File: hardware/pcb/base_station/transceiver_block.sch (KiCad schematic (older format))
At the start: 22 parts, among them CON5 RJ45_TART, CON6 RJ45_TART, IC13 LTC2851, IC14 LTC2851, IC15 LTC2851, IC16 LTC2851, IC17 LTC2851, IC18 LTC2851

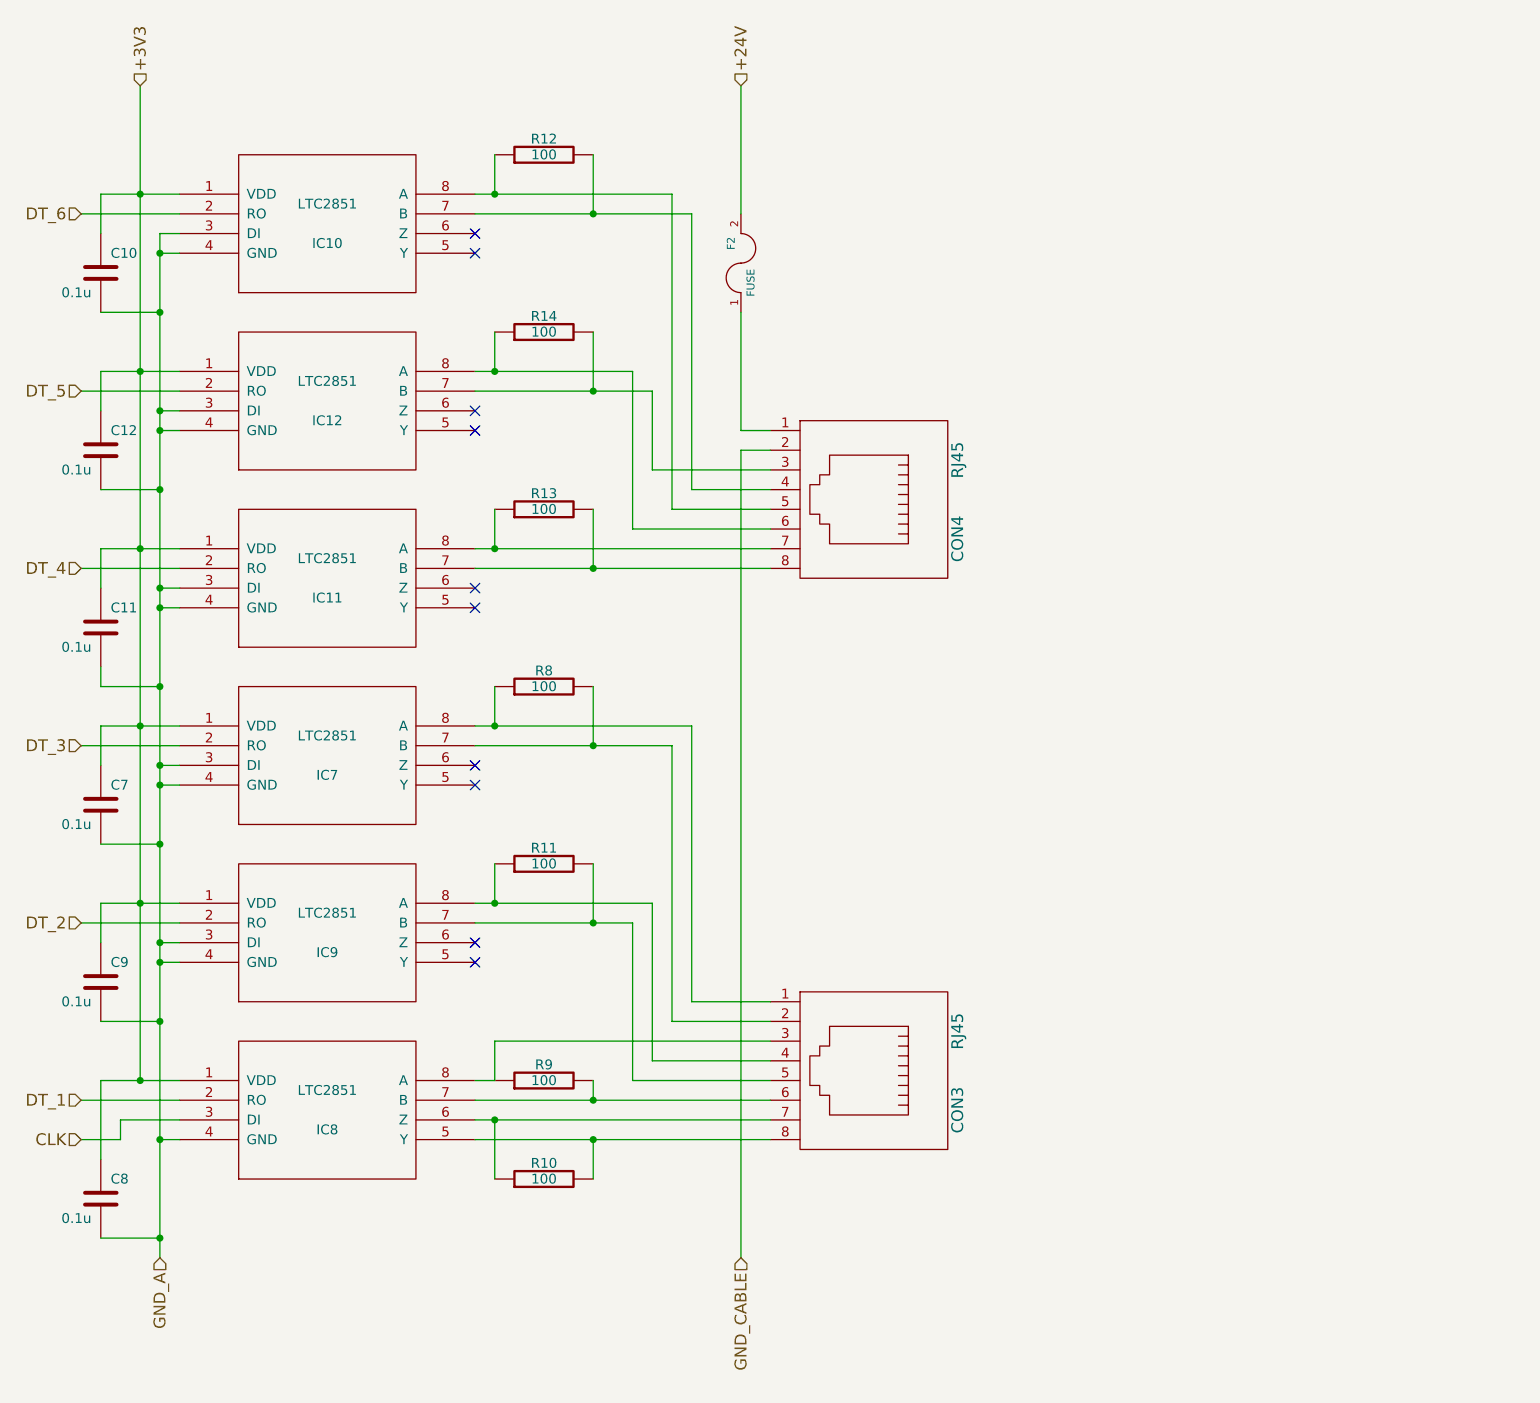
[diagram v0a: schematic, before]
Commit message: Moved things around so that old files are in the legacy directory
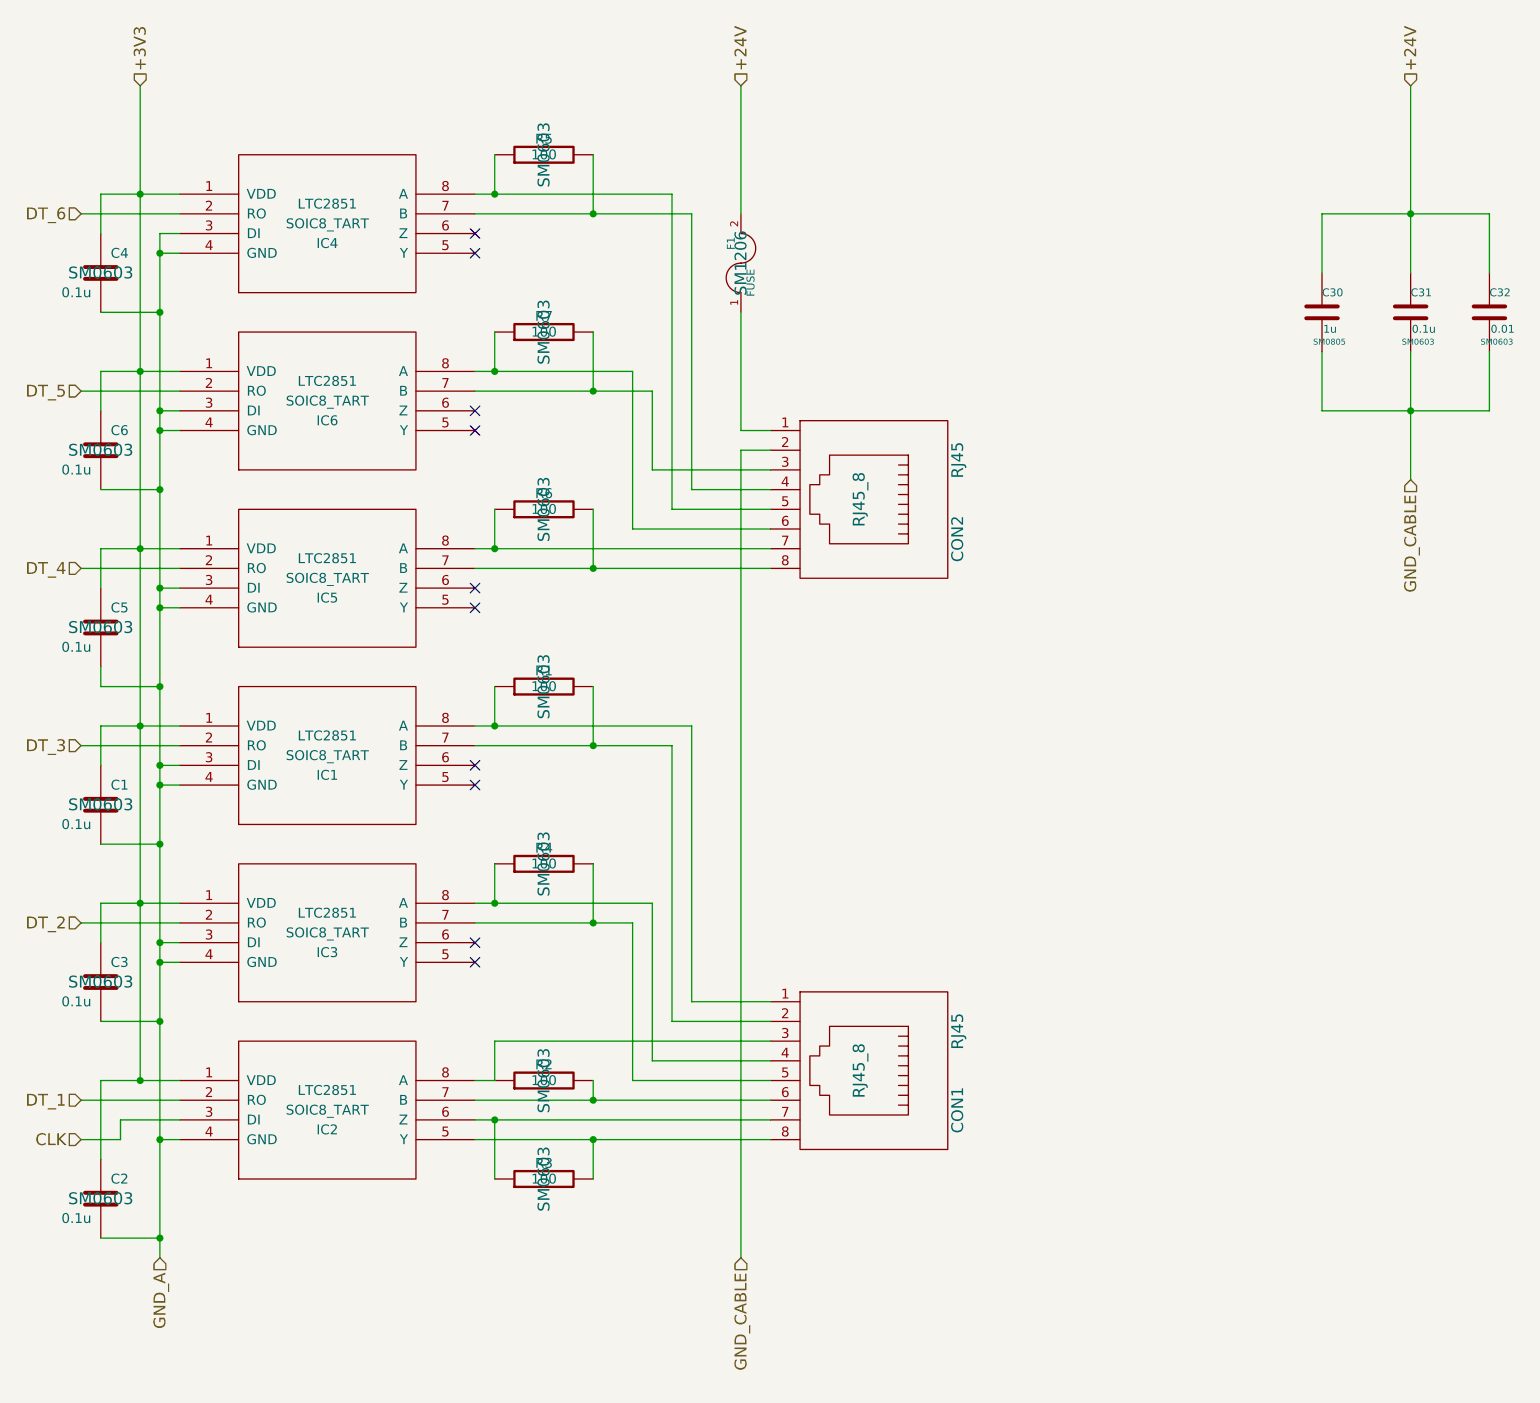
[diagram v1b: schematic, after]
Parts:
- added C36: 1u, SM0805, symbol C
- added C37: 0.1u, SM0603, symbol C
- added C38: 0.01, SM0603, symbol C
- C13, C14, C15, C16, C17, C18, R15, R16, R17, R18, R19, R20, R21: footprint (none) -> SM0603
- CON5, CON6: footprint (none) -> RJ45_8
- F1: footprint ~ -> SM1206
- IC13, IC14, IC15, IC16, IC17, IC18: footprint MODULE -> SOIC8_TART
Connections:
- net +24V: now also C36.1, C37.1, C38.1
- net GND_CABLE: now also C36.2, C37.2, C38.2
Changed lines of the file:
@@
 $Descr A4 11693 8268
 encoding utf-8
-Sheet 5 7
+Sheet 4 7
 Title ""
-Date "8 dec 2014"
+Date "13 feb 2015"
 Rev ""
 Comp ""
@@
 AR Path="/54092498/5422055D" Ref="C11"  Part="1"
 AR Path="/540670D5/5422055D" Ref="C23"  Part="1"
-F 0 "C11" H 1850 3900 50  0000 L CNN
+F 0 "C5" H 1850 3900 50  0000 L CNN
 F 1 "0.1u" H 1600 3700 50  0000 L CNN
-F 2 "" H 1800 3800 60  0001 C CNN
+F 2 "SM0603" H 1800 3800 60  0000 C CNN
 F 3 "" H 1800 3800 60  0001 C CNN
 	1    1800 3800
@@
 AR Path="/54092498/5418D866" Ref="CON3"  Part="1"
 AR Path="/540670D5/5418D866" Ref="CON7"  Part="1"
-F 0 "CON3" H 5850 6550 60  0000 C CNN
+F 0 "CON1" H 5850 6550 60  0000 C CNN
 F 1 "RJ45_TART" H 6250 6600 60  0001 C CNN
-F 2 "" H 5650 6050 60  0001 C CNN
+F 2 "RJ45_8" H 5650 6050 60  0000 C CNN
 F 3 "" H 5650 6050 60  0001 C CNN
 F 4 "STEWART CONNECTOR" H 6650 6500 60  0001 C CNN "MANUFAC"
@@
 AR Path="/54092498/5418D832" Ref="CON4"  Part="1"
 AR Path="/540670D5/5418D832" Ref="CON8"  Part="1"
-F 0 "CON4" H 5850 3650 60  0000 C CNN
+F 0 "CON2" H 5850 3650 60  0000 C CNN
 F 1 "RJ45_TART" H 6250 3700 60  0001 C CNN
-F 2 "" H 5650 3150 60  0001 C CNN
+F 2 "RJ45_8" H 5650 3150 60  0000 C CNN
 F 3 "" H 5650 3150 60  0001 C CNN
 F 4 "STEWART CONNECTOR" H 6650 3600 60  0001 C CNN "MANUFAC"
@@
 AR Path="/54092498/540678BD" Ref="R12"  Part="1"
 AR Path="/540670D5/540678BD" Ref="R26"  Part="1"
-F 0 "R12" V 4130 1400 50  0000 C CNN
+F 0 "R5" V 4130 1400 50  0000 C CNN
 F 1 "100" V 4050 1400 50  0000 C CNN
-F 2 "" H 4050 1400 60  0001 C CNN
+F 2 "SM0603" H 4050 1400 60  0000 C CNN
 F 3 "" H 4050 1400 60  0001 C CNN
 	1    4050 1400
@@
 AR Path="/54092498/540678A5" Ref="R14"  Part="1"
 AR Path="/540670D5/540678A5" Ref="R28"  Part="1"
-F 0 "R14" V 4130 2300 50  0000 C CNN
+F 0 "R7" V 4130 2300 50  0000 C CNN
 F 1 "100" V 4050 2300 50  0000 C CNN
-F 2 "" H 4050 2300 60  0001 C CNN
+F 2 "SM0603" H 4050 2300 60  0000 C CNN
 F 3 "" H 4050 2300 60  0001 C CNN
 	1    4050 2300
@@
 AR Path="/54092498/5406788C" Ref="R13"  Part="1"
 AR Path="/540670D5/5406788C" Ref="R27"  Part="1"
-F 0 "R13" V 4130 3200 50  0000 C CNN
+F 0 "R6" V 4130 3200 50  0000 C CNN
 F 1 "100" V 4050 3200 50  0000 C CNN
-F 2 "" H 4050 3200 60  0001 C CNN
+F 2 "SM0603" H 4050 3200 60  0000 C CNN
 F 3 "" H 4050 3200 60  0001 C CNN
 	1    4050 3200
@@
 AR Path="/54092498/54067855" Ref="R8"  Part="1"
 AR Path="/540670D5/54067855" Ref="R22"  Part="1"
-F 0 "R8" V 4130 4100 50  0000 C CNN
+F 0 "R1" V 4130 4100 50  0000 C CNN
 F 1 "100" V 4050 4100 50  0000 C CNN
-F 2 "" H 4050 4100 60  0001 C CNN
+F 2 "SM0603" H 4050 4100 60  0000 C CNN
 F 3 "" H 4050 4100 60  0001 C CNN
 	1    4050 4100
@@
 AR Path="/54092498/540677FC" Ref="R11"  Part="1"
 AR Path="/540670D5/540677FC" Ref="R25"  Part="1"
-F 0 "R11" V 4130 5000 50  0000 C CNN
+F 0 "R4" V 4130 5000 50  0000 C CNN
 F 1 "100" V 4050 5000 50  0000 C CNN
-F 2 "" H 4050 5000 60  0001 C CNN
+F 2 "SM0603" H 4050 5000 60  0000 C CNN
 F 3 "" H 4050 5000 60  0001 C CNN
 	1    4050 5000
@@
 AR Path="/54092498/54067578" Ref="IC8"  Part="1"
 AR Path="/540670D5/54067578" Ref="IC20"  Part="1"
-F 0 "IC8" H 2950 6150 50  0000 C CNN
+F 0 "IC2" H 2950 6150 50  0000 C CNN
 F 1 "LTC2851" H 2950 6350 50  0000 C CNN
-F 2 "MODULE" H 2950 6250 50  0001 C CNN
+F 2 "SOIC8_TART" H 2950 6250 50  0000 C CNN
 F 3 "DOCUMENTATION" H 2950 6250 50  0001 C CNN
 	1    2950 6250
@@
 AR Path="/54092498/54067576" Ref="IC9"  Part="1"
 AR Path="/540670D5/54067576" Ref="IC21"  Part="1"
-F 0 "IC9" H 2950 5250 50  0000 C CNN
+F 0 "IC3" H 2950 5250 50  0000 C CNN
 F 1 "LTC2851" H 2950 5450 50  0000 C CNN
-F 2 "MODULE" H 2950 5350 50  0001 C CNN
+F 2 "SOIC8_TART" H 2950 5350 50  0000 C CNN
 F 3 "DOCUMENTATION" H 2950 5350 50  0001 C CNN
 	1    2950 5350
@@
 AR Path="/54092498/54067575" Ref="IC7"  Part="1"
 AR Path="/540670D5/54067575" Ref="IC19"  Part="1"
-F 0 "IC7" H 2950 4350 50  0000 C CNN
+F 0 "IC1" H 2950 4350 50  0000 C CNN
 F 1 "LTC2851" H 2950 4550 50  0000 C CNN
-F 2 "MODULE" H 2950 4450 50  0001 C CNN
+F 2 "SOIC8_TART" H 2950 4450 50  0000 C CNN
 F 3 "DOCUMENTATION" H 2950 4450 50  0001 C CNN
 	1    2950 4450
@@
 AR Path="/54092498/54067574" Ref="R9"  Part="1"
 AR Path="/540670D5/54067574" Ref="R23"  Part="1"
-F 0 "R9" V 4130 6100 50  0000 C CNN
+F 0 "R2" V 4130 6100 50  0000 C CNN
 F 1 "100" V 4050 6100 50  0000 C CNN
-F 2 "" H 4050 6100 60  0001 C CNN
+F 2 "SM0603" H 4050 6100 60  0000 C CNN
 F 3 "" H 4050 6100 60  0001 C CNN
 	1    4050 6100
@@
 AR Path="/54092498/54067573" Ref="R10"  Part="1"
 AR Path="/540670D5/54067573" Ref="R24"  Part="1"
-F 0 "R10" V 4130 6600 50  0000 C CNN
+F 0 "R3" V 4130 6600 50  0000 C CNN
 F 1 "100" V 4050 6600 50  0000 C CNN
-F 2 "" H 4050 6600 60  0001 C CNN
+F 2 "SM0603" H 4050 6600 60  0000 C CNN
 F 3 "" H 4050 6600 60  0001 C CNN
 	1    4050 6600
@@
 AR Path="/54092498/54067570" Ref="IC11"  Part="1"
 AR Path="/540670D5/54067570" Ref="IC23"  Part="1"
-F 0 "IC11" H 2950 3450 50  0000 C CNN
+F 0 "IC5" H 2950 3450 50  0000 C CNN
 F 1 "LTC2851" H 2950 3650 50  0000 C CNN
-F 2 "MODULE" H 2950 3550 50  0001 C CNN
+F 2 "SOIC8_TART" H 2950 3550 50  0000 C CNN
 F 3 "DOCUMENTATION" H 2950 3550 50  0001 C CNN
 	1    2950 3550
@@
 AR Path="/54092498/5406756F" Ref="IC12"  Part="1"
 AR Path="/540670D5/5406756F" Ref="IC24"  Part="1"
-F 0 "IC12" H 2950 2550 50  0000 C CNN
+F 0 "IC6" H 2950 2550 50  0000 C CNN
 F 1 "LTC2851" H 2950 2750 50  0000 C CNN
-F 2 "MODULE" H 2950 2650 50  0001 C CNN
+F 2 "SOIC8_TART" H 2950 2650 50  0000 C CNN
 F 3 "DOCUMENTATION" H 2950 2650 50  0001 C CNN
 	1    2950 2650
@@
 AR Path="/54092498/5406756E" Ref="IC10"  Part="1"
 AR Path="/540670D5/5406756E" Ref="IC22"  Part="1"
-F 0 "IC10" H 2950 1650 50  0000 C CNN
+F 0 "IC4" H 2950 1650 50  0000 C CNN
 F 1 "LTC2851" H 2950 1850 50  0000 C CNN
-F 2 "MODULE" H 2950 1750 50  0001 C CNN
+F 2 "SOIC8_TART" H 2950 1750 50  0000 C CNN
 F 3 "DOCUMENTATION" H 2950 1750 50  0001 C CNN
 	1    2950 1750
@@
 AR Path="/54092498/5406756A" Ref="C10"  Part="1"
 AR Path="/540670D5/5406756A" Ref="C22"  Part="1"
-F 0 "C10" H 1850 2100 50  0000 L CNN
+F 0 "C4" H 1850 2100 50  0000 L CNN
 F 1 "0.1u" H 1600 1900 50  0000 L CNN
-F 2 "" H 1800 2000 60  0001 C CNN
+F 2 "SM0603" H 1800 2000 60  0000 C CNN
 F 3 "" H 1800 2000 60  0001 C CNN
 	1    1800 2000
@@
 AR Path="/54092498/54067569" Ref="C12"  Part="1"
 AR Path="/540670D5/54067569" Ref="C24"  Part="1"
-F 0 "C12" H 1850 3000 50  0000 L CNN
+F 0 "C6" H 1850 3000 50  0000 L CNN
 F 1 "0.1u" H 1600 2800 50  0000 L CNN
-F 2 "" H 1800 2900 60  0001 C CNN
+F 2 "SM0603" H 1800 2900 60  0000 C CNN
 F 3 "" H 1800 2900 60  0001 C CNN
 	1    1800 2900
@@
 AR Path="/54092498/54067568" Ref="C7"  Part="1"
 AR Path="/540670D5/54067568" Ref="C19"  Part="1"
-F 0 "C7" H 1850 4800 50  0000 L CNN
+F 0 "C1" H 1850 4800 50  0000 L CNN
 F 1 "0.1u" H 1600 4600 50  0000 L CNN
-F 2 "" H 1800 4700 60  0001 C CNN
+F 2 "SM0603" H 1800 4700 60  0000 C CNN
 F 3 "" H 1800 4700 60  0001 C CNN
 	1    1800 4700
@@
 AR Path="/54092498/54067567" Ref="C9"  Part="1"
 AR Path="/540670D5/54067567" Ref="C21"  Part="1"
-F 0 "C9" H 1850 5700 50  0000 L CNN
+F 0 "C3" H 1850 5700 50  0000 L CNN
 F 1 "0.1u" H 1600 5500 50  0000 L CNN
-F 2 "" H 1800 5600 60  0001 C CNN
+F 2 "SM0603" H 1800 5600 60  0000 C CNN
 F 3 "" H 1800 5600 60  0001 C CNN
 	1    1800 5600
@@
 AR Path="/54092498/54067566" Ref="C8"  Part="1"
 AR Path="/540670D5/54067566" Ref="C20"  Part="1"
-F 0 "C8" H 1850 6800 50  0000 L CNN
+F 0 "C2" H 1850 6800 50  0000 L CNN
 F 1 "0.1u" H 1600 6600 50  0000 L CNN
-F 2 "" H 1800 6700 60  0001 C CNN
+F 2 "SM0603" H 1800 6700 60  0000 C CNN
 F 3 "" H 1800 6700 60  0001 C CNN
 	1    1800 6700
@@
 AR Path="/5409247B/54257C9F" Ref="F3"  Part="1"
 AR Path="/540670D5/54257C9F" Ref="F4"  Part="1"
-F 0 "F2" H 5150 2000 40  0000 C CNN
+F 0 "F1" H 5150 2000 40  0000 C CNN
 F 1 "FUSE" H 4950 1900 40  0000 C CNN
-F 2 "~" H 5050 1950 60  0000 C CNN
+F 2 "SM1206" H 5050 1950 60  0000 C CNN
 F 3 "~" H 5050 1950 60  0000 C CNN
 	1    5050 1950
@@
 Wire Wire Line
 	5050 1700 5050 1050
+$Comp
+L C C36
+U 1 1 54D93965
+P 8000 2200
+AR Path="/540670D5/54D93965" Ref="C36"  Part="1"
+AR Path="/5409247B/54D93965" Ref="C27"  Part="1"
+AR Path="/540924B7/54D93965" Ref="C30"  Part="1"
+AR Path="/54092498/54D93965" Ref="C33"  Part="1"
+F 0 "C30" H 8000 2300 40  0000 L CNN
+F 1 "1u" H 8006 2115 40  0000 L CNN
+F 2 "SM0805" H 8038 2050 30  0000 C CNN
+F 3 "~" H 8000 2200 60  0000 C CNN
+	1    8000 2200
+	1    0    0    -1
+$EndComp
+$Comp
+L C C37
+U 1 1 54D93974
+P 8450 2200
+AR Path="/540670D5/54D93974" Ref="C37"  Part="1"
+AR Path="/5409247B/54D93974" Ref="C28"  Part="1"
+AR Path="/540924B7/54D93974" Ref="C31"  Part="1"
+AR Path="/54092498/54D93974" Ref="C34"  Part="1"
+F 0 "C31" H 8450 2300 40  0000 L CNN
+F 1 "0.1u" H 8456 2115 40  0000 L CNN
+F 2 "SM0603" H 8488 2050 30  0000 C CNN
+F 3 "~" H 8450 2200 60  0000 C CNN
+	1    8450 2200
+	1    0    0    -1
+$EndComp
+$Comp
+L C C38
+U 1 1 54D93983
+P 8850 2200
+AR Path="/540670D5/54D93983" Ref="C38"  Part="1"
+AR Path="/5409247B/54D93983" Ref="C29"  Part="1"
+AR Path="/540924B7/54D93983" Ref="C32"  Part="1"
+AR Path="/54092498/54D93983" Ref="C35"  Part="1"
+F 0 "C32" H 8850 2300 40  0000 L CNN
+F 1 "0.01" H 8856 2115 40  0000 L CNN
+F 2 "SM0603" H 8888 2050 30  0000 C CNN
+F 3 "~" H 8850 2200 60  0000 C CNN
+	1    8850 2200
+	1    0    0    -1
+$EndComp
+Text HLabel 8450 1050 1    60   Input ~ 0
++24V
+Text HLabel 8450 3050 3    60   Input ~ 0
+GND_CABLE
+Wire Wire Line
+	8000 2000 8000 1700
+Wire Wire Line
+	8000 1700 8850 1700
+Wire Wire Line
+	8850 1700 8850 2000
+Wire Wire Line
+	8450 1050 8450 2000
+Connection ~ 8450 1700
+Wire Wire Line
+	8000 2400 8000 2700
+Wire Wire Line
+	8000 2700 8850 2700
+Wire Wire Line
+	8850 2700 8850 2400
+Wire Wire Line
+	8450 2400 8450 3050
+Connection ~ 8450 2700
 $EndSCHEMATC
